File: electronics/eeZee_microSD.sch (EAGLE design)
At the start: 10 parts, among them U1 MCP1824S, U2 74HC4050, U4 MICROSD_CD

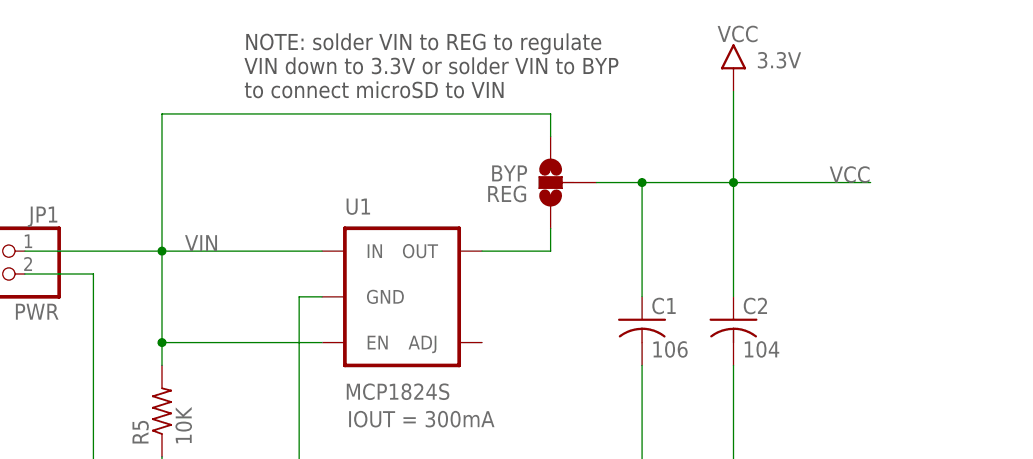
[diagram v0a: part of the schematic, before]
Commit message: Fixed regulator overheat when BYP selected; removed jumper. Regulator outputs 3.3V when VIN=3.3V
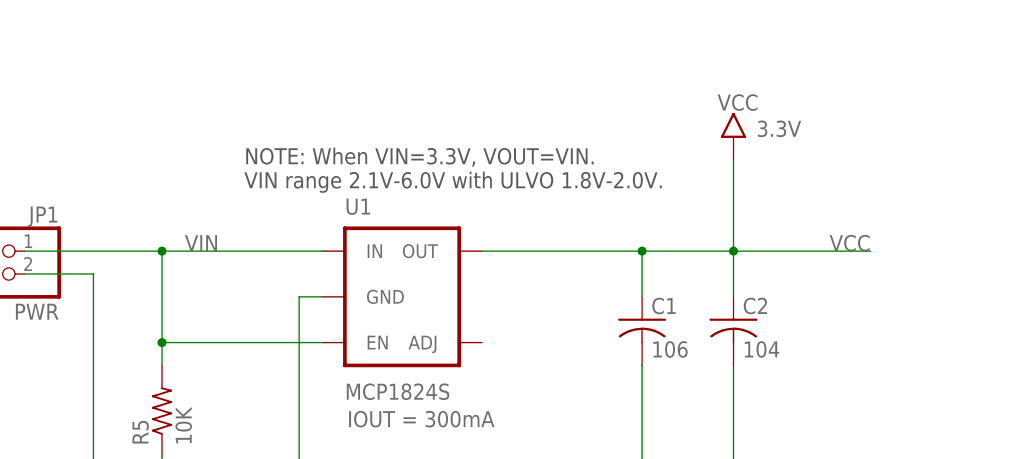
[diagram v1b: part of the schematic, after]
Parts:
- removed REG: BYP, SparkFun:SOLDERJUMPER_2WAYS
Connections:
- removed net N$1: REG.1, U1.OUT
- net VCC: now also U1.OUT; no longer REG.2
- net VIN: no longer REG.3
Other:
- note added: "NOTE: When VIN=3.3V, VOUT=VIN. VIN range 2.1V-6.0V with ULVO 1.8V-2.0V."
- note removed: "NOTE: solder VIN to REG to regulate VIN down to 3.3V or solder VIN to BYP to connect microSD to VIN"
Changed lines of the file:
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@@
 <part name="JP3" library="pinhead-2" deviceset="PINHD-1X05" device="_2.54-S"/>
 <part name="U4" library="bt_electromech" deviceset="MICROSD_CD" device=""/>
-<part name="REG" library="SparkFun" deviceset="SOLDERJUMPER_2WAY" device="S" value="BYP"/>
 </parts>
 <sheets>
 <sheet>
 <plain>
-<text x="115.824" y="173.99" size="1.778" layer="97" align="top-left">NOTE: solder VIN to REG to regulate
-VIN down to 3.3V or solder VIN to BYP
-to connect microSD to VIN</text>
+<text x="115.824" y="161.29" size="1.778" layer="97" align="top-left">NOTE: When VIN=3.3V, VOUT=VIN.
+VIN range 2.1V-6.0V with ULVO 1.8V-2.0V.</text>
 <text x="153.924" y="23.114" size="3.81" layer="94">eeZee microSD</text>
 <text x="231.14" y="22.86" size="3.81" layer="94">0.4B</text>
@@
 </instance>
 <instance part="GND5" gate="1" x="119.38" y="38.1"/>
-<instance part="U$2" gate="G$1" x="170.18" y="167.64"/>
+<instance part="U$2" gate="G$1" x="170.18" y="160.02"/>
 <instance part="U$3" gate="G$1" x="119.38" y="91.44"/>
 <instance part="U$4" gate="G$1" x="43.18" y="88.9"/>
@@
 <instance part="JP3" gate="A" x="200.66" y="88.9"/>
 <instance part="U4" gate="U1" x="25.4" y="66.04"/>
-<instance part="REG" gate="G$1" x="149.86" y="157.48" rot="R180"/>
 </instances>
 <busses>
@@
 <junction x="106.68" y="139.7"/>
 <junction x="106.68" y="149.86"/>
-<pinref part="REG" gate="G$1" pin="3"/>
-<wire x1="149.86" y1="162.56" x2="149.86" y2="165.1" width="0.1524" layer="91"/>
-<wire x1="149.86" y1="165.1" x2="106.68" y2="165.1" width="0.1524" layer="91"/>
-<wire x1="106.68" y1="165.1" x2="106.68" y2="149.86" width="0.1524" layer="91"/>
 </segment>
 </net>
@@
 <net name="VCC" class="0">
 <segment>
-<wire x1="154.94" y1="157.48" x2="160.02" y2="157.48" width="0.1524" layer="91"/>
-<wire x1="160.02" y1="144.78" x2="160.02" y2="157.48" width="0.1524" layer="91"/>
+<wire x1="160.02" y1="144.78" x2="160.02" y2="149.86" width="0.1524" layer="91"/>
 <pinref part="C1" gate="G$1" pin="1"/>
-<junction x="160.02" y="157.48"/>
-<wire x1="160.02" y1="157.48" x2="170.18" y2="157.48" width="0.1524" layer="91"/>
-<label x="185.42" y="157.48" size="1.778" layer="95" rot="MR0"/>
-<wire x1="170.18" y1="157.48" x2="185.42" y2="157.48" width="0.1524" layer="91"/>
-<junction x="170.18" y="157.48"/>
+<junction x="160.02" y="149.86"/>
+<wire x1="160.02" y1="149.86" x2="170.18" y2="149.86" width="0.1524" layer="91"/>
+<label x="185.42" y="149.86" size="1.778" layer="95" rot="MR0"/>
+<wire x1="170.18" y1="149.86" x2="185.42" y2="149.86" width="0.1524" layer="91"/>
+<junction x="170.18" y="149.86"/>
 <pinref part="C2" gate="G$1" pin="1"/>
-<wire x1="170.18" y1="144.78" x2="170.18" y2="157.48" width="0.1524" layer="91"/>
+<wire x1="170.18" y1="144.78" x2="170.18" y2="149.86" width="0.1524" layer="91"/>
 <pinref part="U$2" gate="G$1" pin="VCC"/>
-<wire x1="170.18" y1="157.48" x2="170.18" y2="167.64" width="0.1524" layer="91"/>
-<pinref part="REG" gate="G$1" pin="2"/>
+<wire x1="170.18" y1="149.86" x2="170.18" y2="160.02" width="0.1524" layer="91"/>
+<pinref part="U1" gate="G$1" pin="OUT"/>
+<wire x1="160.02" y1="149.86" x2="142.24" y2="149.86" width="0.1524" layer="91"/>
 </segment>
 <segment>
@@
 </segment>
 </net>
-<net name="N$1" class="0">
-<segment>
-<pinref part="U1" gate="G$1" pin="OUT"/>
-<pinref part="REG" gate="G$1" pin="1"/>
-<wire x1="142.24" y1="149.86" x2="149.86" y2="149.86" width="0.1524" layer="91"/>
-<wire x1="149.86" y1="149.86" x2="149.86" y2="152.4" width="0.1524" layer="91"/>
-</segment>
-</net>

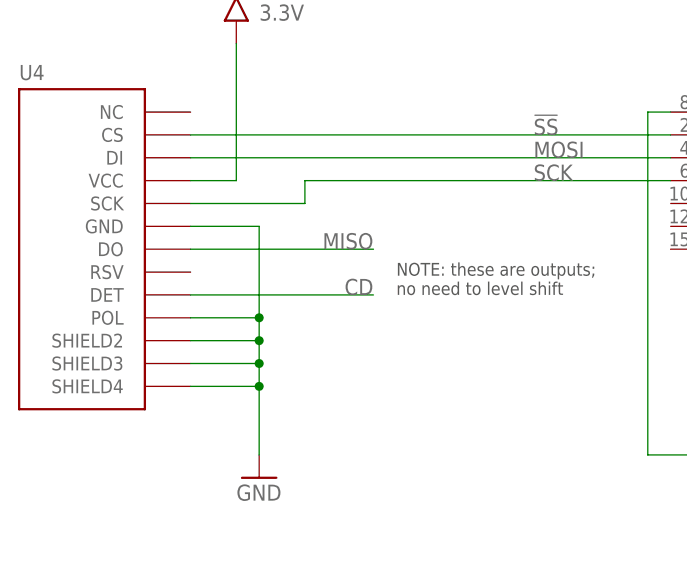
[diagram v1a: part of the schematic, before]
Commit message: board rerouting, layout, etc., to accommodate solder jumper that was removed
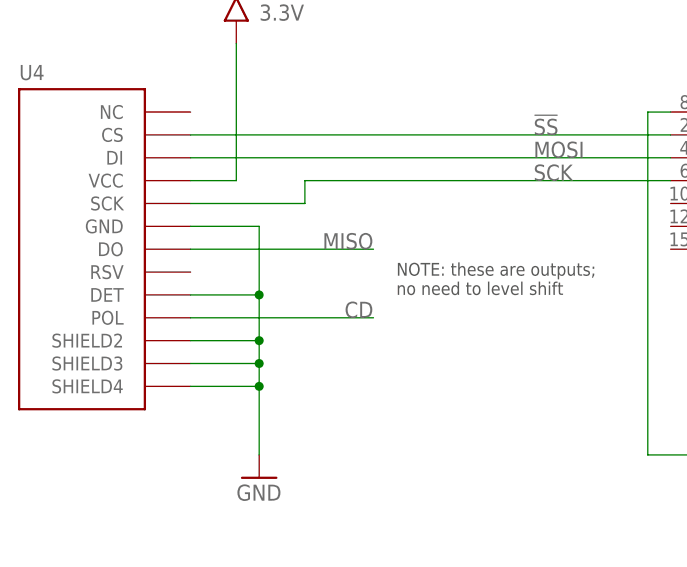
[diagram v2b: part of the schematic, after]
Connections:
- net CD: now also U4.POL; no longer U4.DET
- net GND: now also U4.DET; no longer U4.POL
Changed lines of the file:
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@@
 <segment>
 <wire x1="38.1" y1="68.58" x2="45.72" y2="68.58" width="0.1524" layer="91"/>
-<wire x1="45.72" y1="68.58" x2="45.72" y2="58.42" width="0.1524" layer="91"/>
-<wire x1="38.1" y1="58.42" x2="45.72" y2="58.42" width="0.1524" layer="91"/>
-<junction x="45.72" y="58.42"/>
-<wire x1="45.72" y1="58.42" x2="45.72" y2="55.88" width="0.1524" layer="91"/>
+<wire x1="45.72" y1="68.58" x2="45.72" y2="60.96" width="0.1524" layer="91"/>
+<wire x1="45.72" y1="60.96" x2="45.72" y2="55.88" width="0.1524" layer="91"/>
 <wire x1="38.1" y1="55.88" x2="45.72" y2="55.88" width="0.1524" layer="91"/>
 <junction x="45.72" y="55.88"/>
@@
 <pinref part="GND1" gate="1" pin="GND"/>
 <pinref part="U4" gate="U1" pin="GND"/>
-<pinref part="U4" gate="U1" pin="POL"/>
 <pinref part="U4" gate="U1" pin="SHIELD2"/>
 <pinref part="U4" gate="U1" pin="SHIELD3"/>
 <pinref part="U4" gate="U1" pin="SHIELD4"/>
+<pinref part="U4" gate="U1" pin="DET"/>
+<wire x1="38.1" y1="60.96" x2="45.72" y2="60.96" width="0.1524" layer="91"/>
+<junction x="45.72" y="60.96"/>
 </segment>
 <segment>
@@
 <net name="CD" class="0">
 <segment>
-<pinref part="U4" gate="U1" pin="DET"/>
-<wire x1="38.1" y1="60.96" x2="58.42" y2="60.96" width="0.1524" layer="91"/>
-<label x="58.42" y="60.96" size="1.778" layer="95" rot="MR0"/>
+<label x="58.42" y="58.42" size="1.778" layer="95" rot="MR0"/>
+<pinref part="U4" gate="U1" pin="POL"/>
+<wire x1="38.1" y1="58.42" x2="58.42" y2="58.42" width="0.1524" layer="91"/>
 </segment>
 <segment>
